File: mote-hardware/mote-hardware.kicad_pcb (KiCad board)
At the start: 2 copper layers, 93.6 x 102.8 mm, 87 parts, among them J1 USB_C_Receptacle_USB2.0_14P, J2 JST_XH2.54-SP, J4 SM03B-SRSS-TB, J5 Conn_01x03_Pin, J6 Conn_01x03_Pin, J7 JST_PH_B6B, J8 JST_PH_B6B, SW1 SW_Push, SW2 SW_Push, U1 RP2354_60QFN, U2 NCP1117-3.3_SOT223, U4 RP Radio Module 2, U5 DRV8833PW, U9 LSM6DS3, Y1 ABM8-272-T3

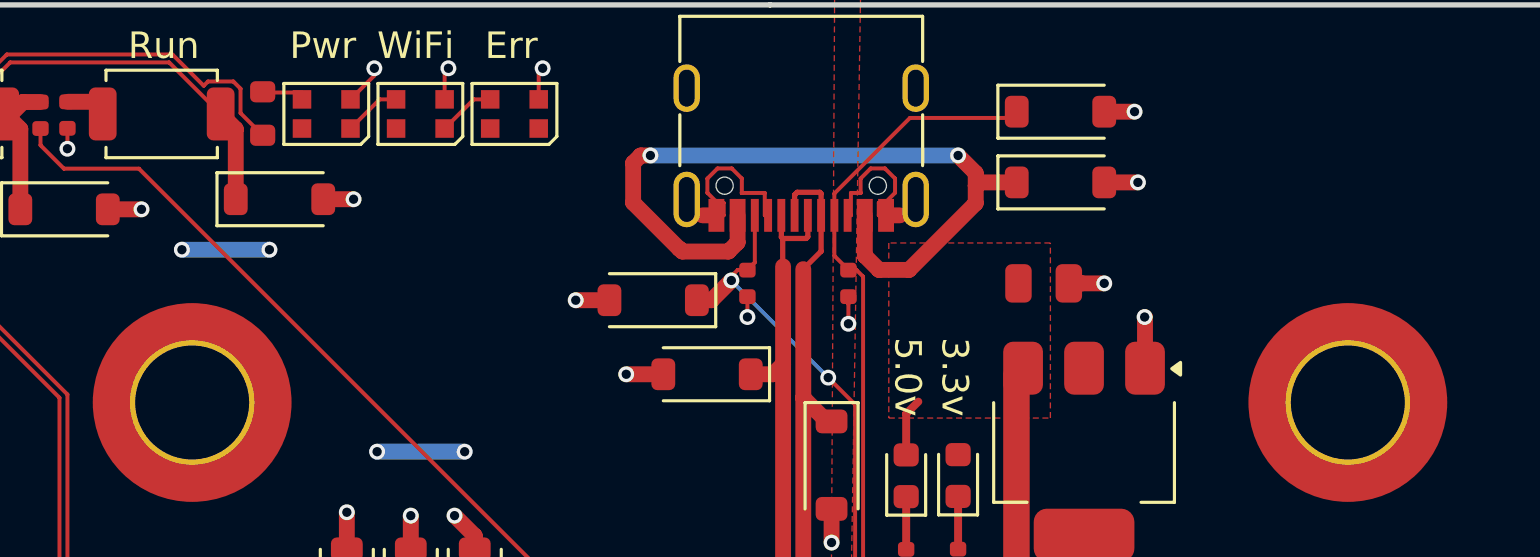
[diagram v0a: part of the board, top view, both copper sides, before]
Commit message: Include tail mount nuts in BOM
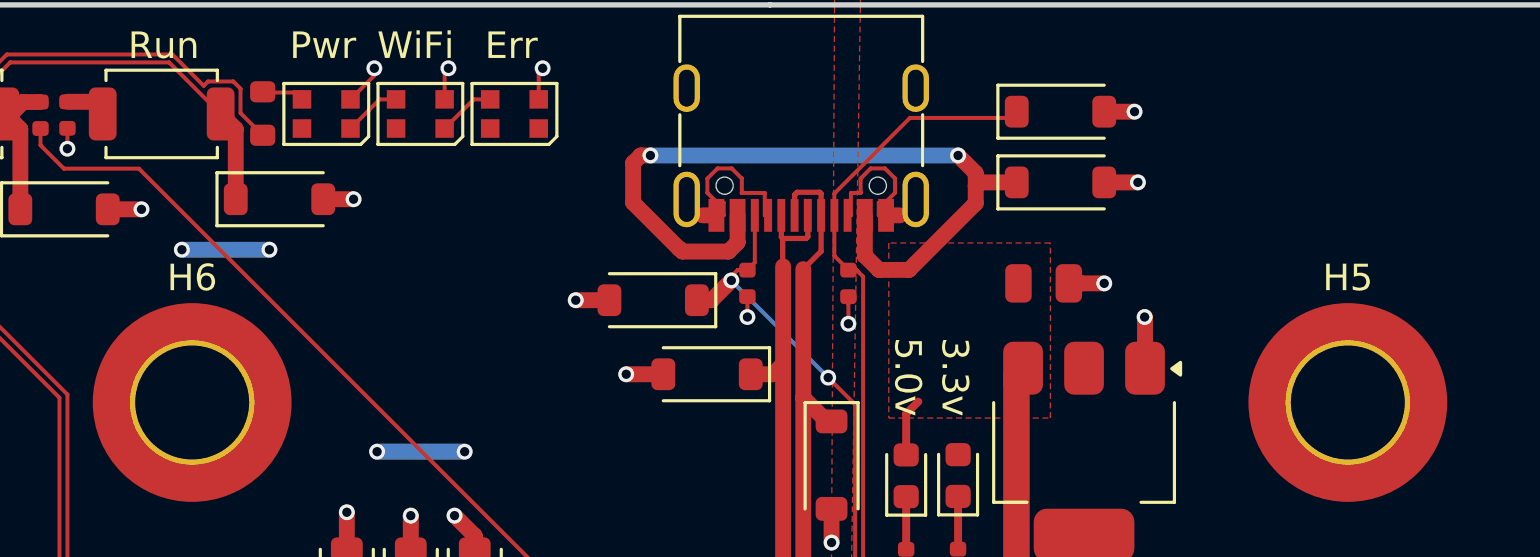
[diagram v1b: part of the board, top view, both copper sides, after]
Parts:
- H5, H6: footprint MountingHole:MountingHole_4.3mm_M4_DIN965_Pad_TopOnly -> mote-hardware:MountingHole_4.3mm_M4_DIN965_Pad_TopOnly
